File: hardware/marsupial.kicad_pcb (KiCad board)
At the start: 4 copper layers, 53.1 x 98 mm, 208 parts, among them J101 DC IN, J102 DC OUT, J103 FPC, J201 USB_C_Receptacle_USB2.0, J301 MANUAL, J401 TagConnect, J501 MANUAL, J601 USB_C_Receptacle_USB2.0, J701 USB_C_Receptacle_USB2.0, Q201 DMP3028, Q202 DMP3028, Q203 DMP3028, Q204 MMBT3904, Q205 MMBT3904, Q206 DMP3028, Q207 MMBT3904, Q401 AO3400A, Q402 AO3400A, Q601 DMP3028, Q602 DMP3028, Q603 DMP3028, Q604 MMBT3904, Q605 MMBT3904, Q606 DMP3028, Q607 MMBT3904, SW1 RESET, U101 HT7550-1, U102 XC6206, U201 SRV05-4, U202 INA381A2IDSGR, U203 BL1551B, U301 SiC437, U401 STM32G071RBTx, U501 SiC437, U601 SRV05-4, U602 INA381A2IDSGR, U603 BL1551B, U701 USB2412-DZK-TR, Y401 12MHz, Y701 24MHz

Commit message: finish artwork
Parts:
- moved J103 6.61 mm to (155.4, 102.3), turned to 90 degrees
- moved G*** 5.29 mm to (145.8, 101.0), turned to -5 degrees
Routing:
- net /USB1_DM: track 105.1 -> 110.2 mm
- net /USB1_DP: track 103.7 -> 108.7 mm
- net /USB2_DM: track 105.5 -> 110.0 mm
- net /USB2_DP: track 108.8 -> 113.1 mm
- net GND: vias 136 -> 142

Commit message: Update board art
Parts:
- moved kibuzzard-6664D661 1.02 mm to (116.5, 104.5)
- moved kibuzzard-6664D670 1.02 mm to (119.3, 104.9)
- moved kibuzzard-6664D67C 1.02 mm to (121.9, 104.2)
- moved kibuzzard-6664D680 1.02 mm to (124.1, 104.8)
- moved kibuzzard-6664D691 1.02 mm to (126.6, 104.4)
- moved kibuzzard-6664D696 1.02 mm to (129.2, 104.9)
- moved kibuzzard-6664D69E 1.02 mm to (131.4, 103.9)
- moved kibuzzard-6664D6A2 1.02 mm to (133.3, 104.8)
- moved kibuzzard-6664D6A7 1.02 mm to (135.5, 104.2)
- moved kibuzzard-6664BF3A 0.68 mm to (153.9, 79.8)
- moved G*** 0.12 mm to (145.8, 101.0), turned to -7 degrees

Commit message: clean up drc
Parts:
- moved J103 0.82 mm to (155.0, 101.6)
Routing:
- net /USB1_DM: track 110.2 -> 109.2 mm
- net /USB1_DP: track 108.7 -> 107.7 mm
- net /USB2_DP: track 113.1 -> 112.5 mm
- net /USB2_DM: track 110.0 -> 109.5 mm

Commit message: drc errors?
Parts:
- removed the REF** at (124.0, 67.1)

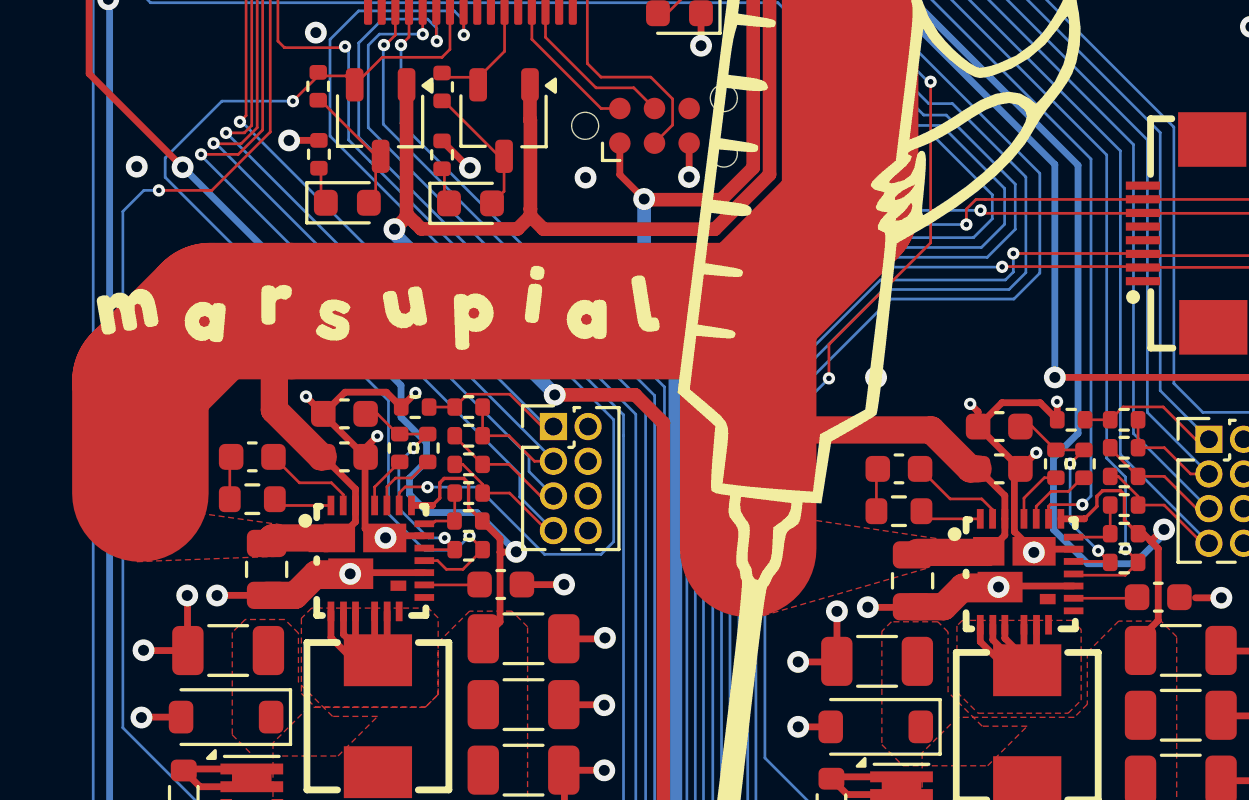
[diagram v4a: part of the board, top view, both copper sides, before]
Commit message: Fix SiC437 footprint and LCSC field error
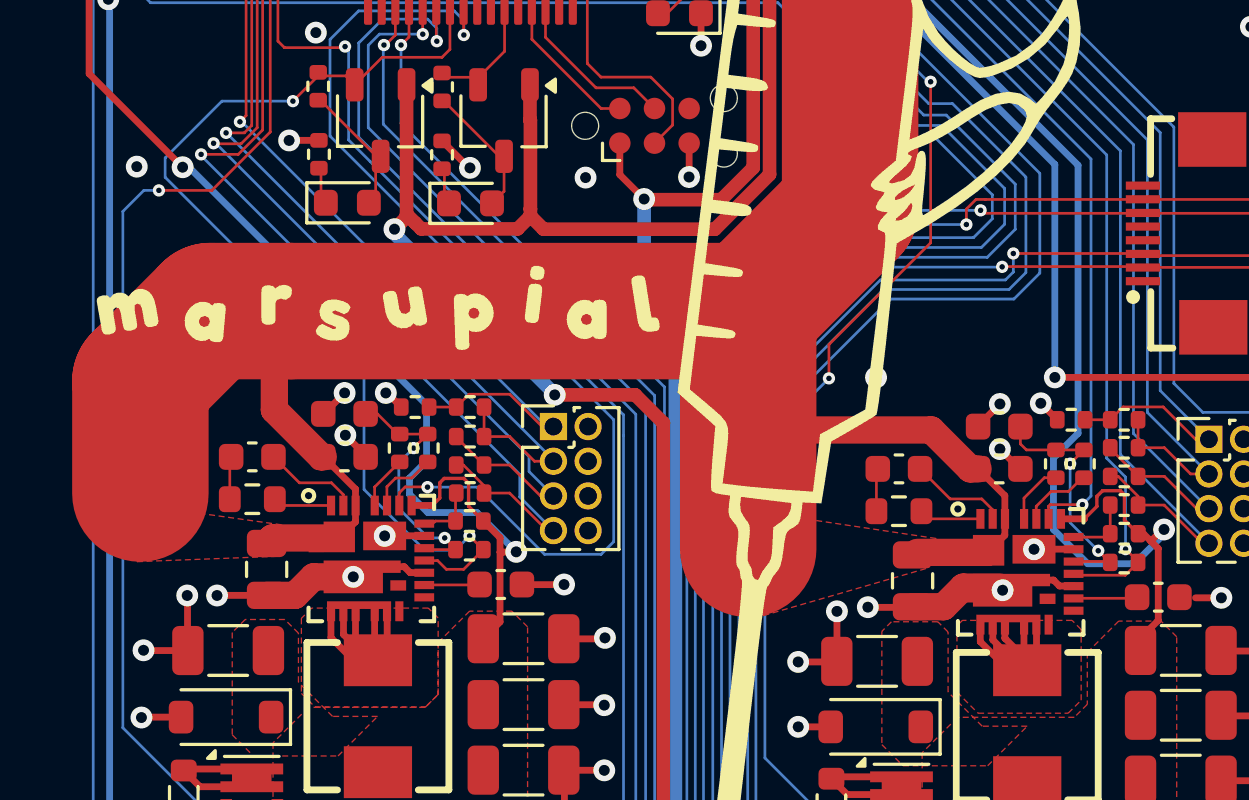
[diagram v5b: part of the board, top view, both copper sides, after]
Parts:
- U301, U501: footprint easyeda2kicad:MLP44-24_L4.0-W4.0-P0.45-TL-EP -> matei:SiC437AED
- moved R308 0.06 mm to (129.0, 109.1)
- moved R307 0.06 mm to (129.0, 110.1)
- moved R306 0.05 mm to (129.0, 111.1)
- moved R309 0.05 mm to (129.0, 108.0)
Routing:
- net /UCPD1_SRC/DC-DC UCPD/AGND_LOCAL: track 13.2 -> 4.50 mm
- net /UCPD2_SRC/DC-DC UCPD/AGND_LOCAL: track 13.1 -> 4.67 mm
